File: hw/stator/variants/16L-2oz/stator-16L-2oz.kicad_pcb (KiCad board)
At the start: 16 copper layers, 175 x 175 mm, 1 part

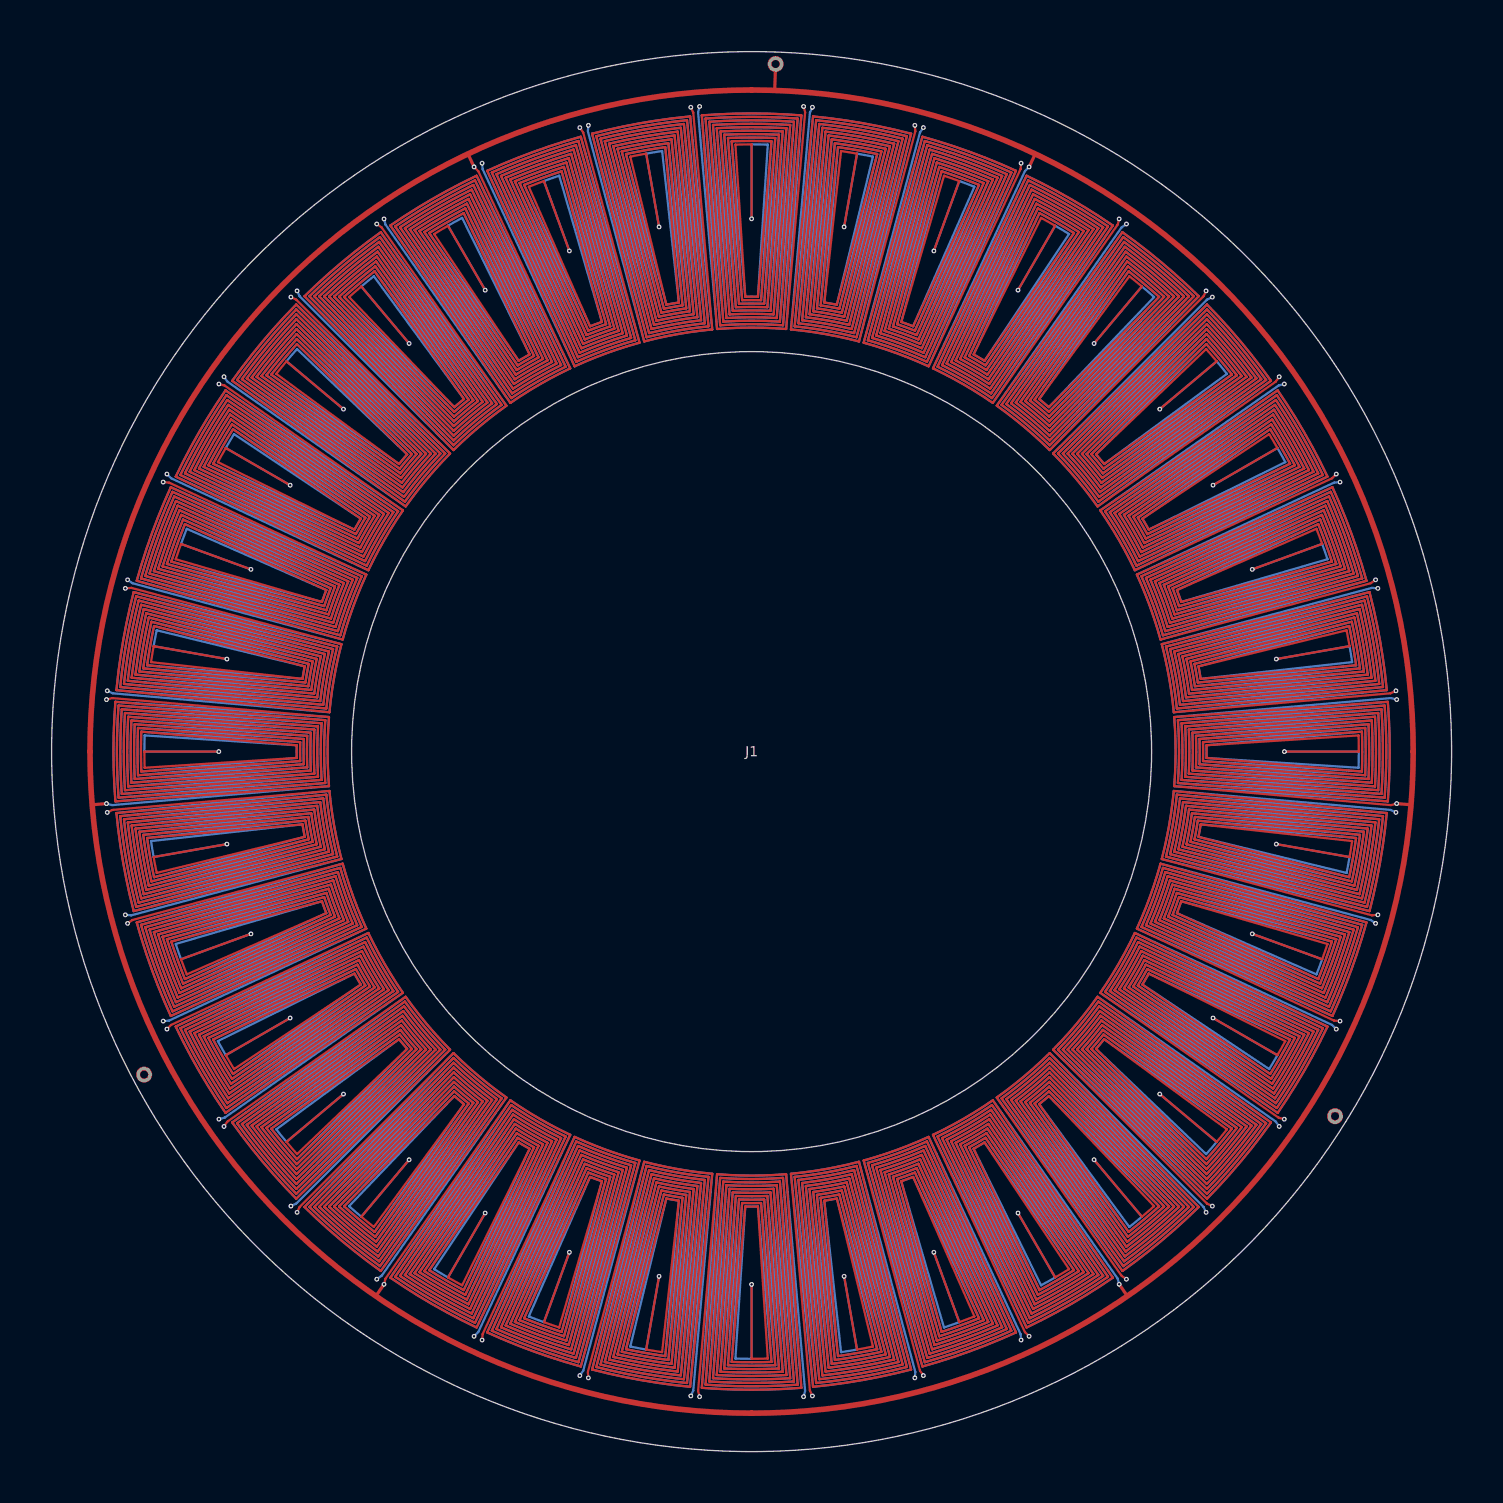
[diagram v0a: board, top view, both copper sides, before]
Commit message: Round 9 in progress: stator layout v2 (coils to r 84.6, +14 % torque), N-S rotor comparison, base as cheap parts, BOM at 20 and 100 units
Co-Authored-By: Claude Fable 5.1 <noreply@anthropic.com>
Claude-Session: https://claude.ai/code/session_01RhbB1sts16H7Chkqp6ycKd
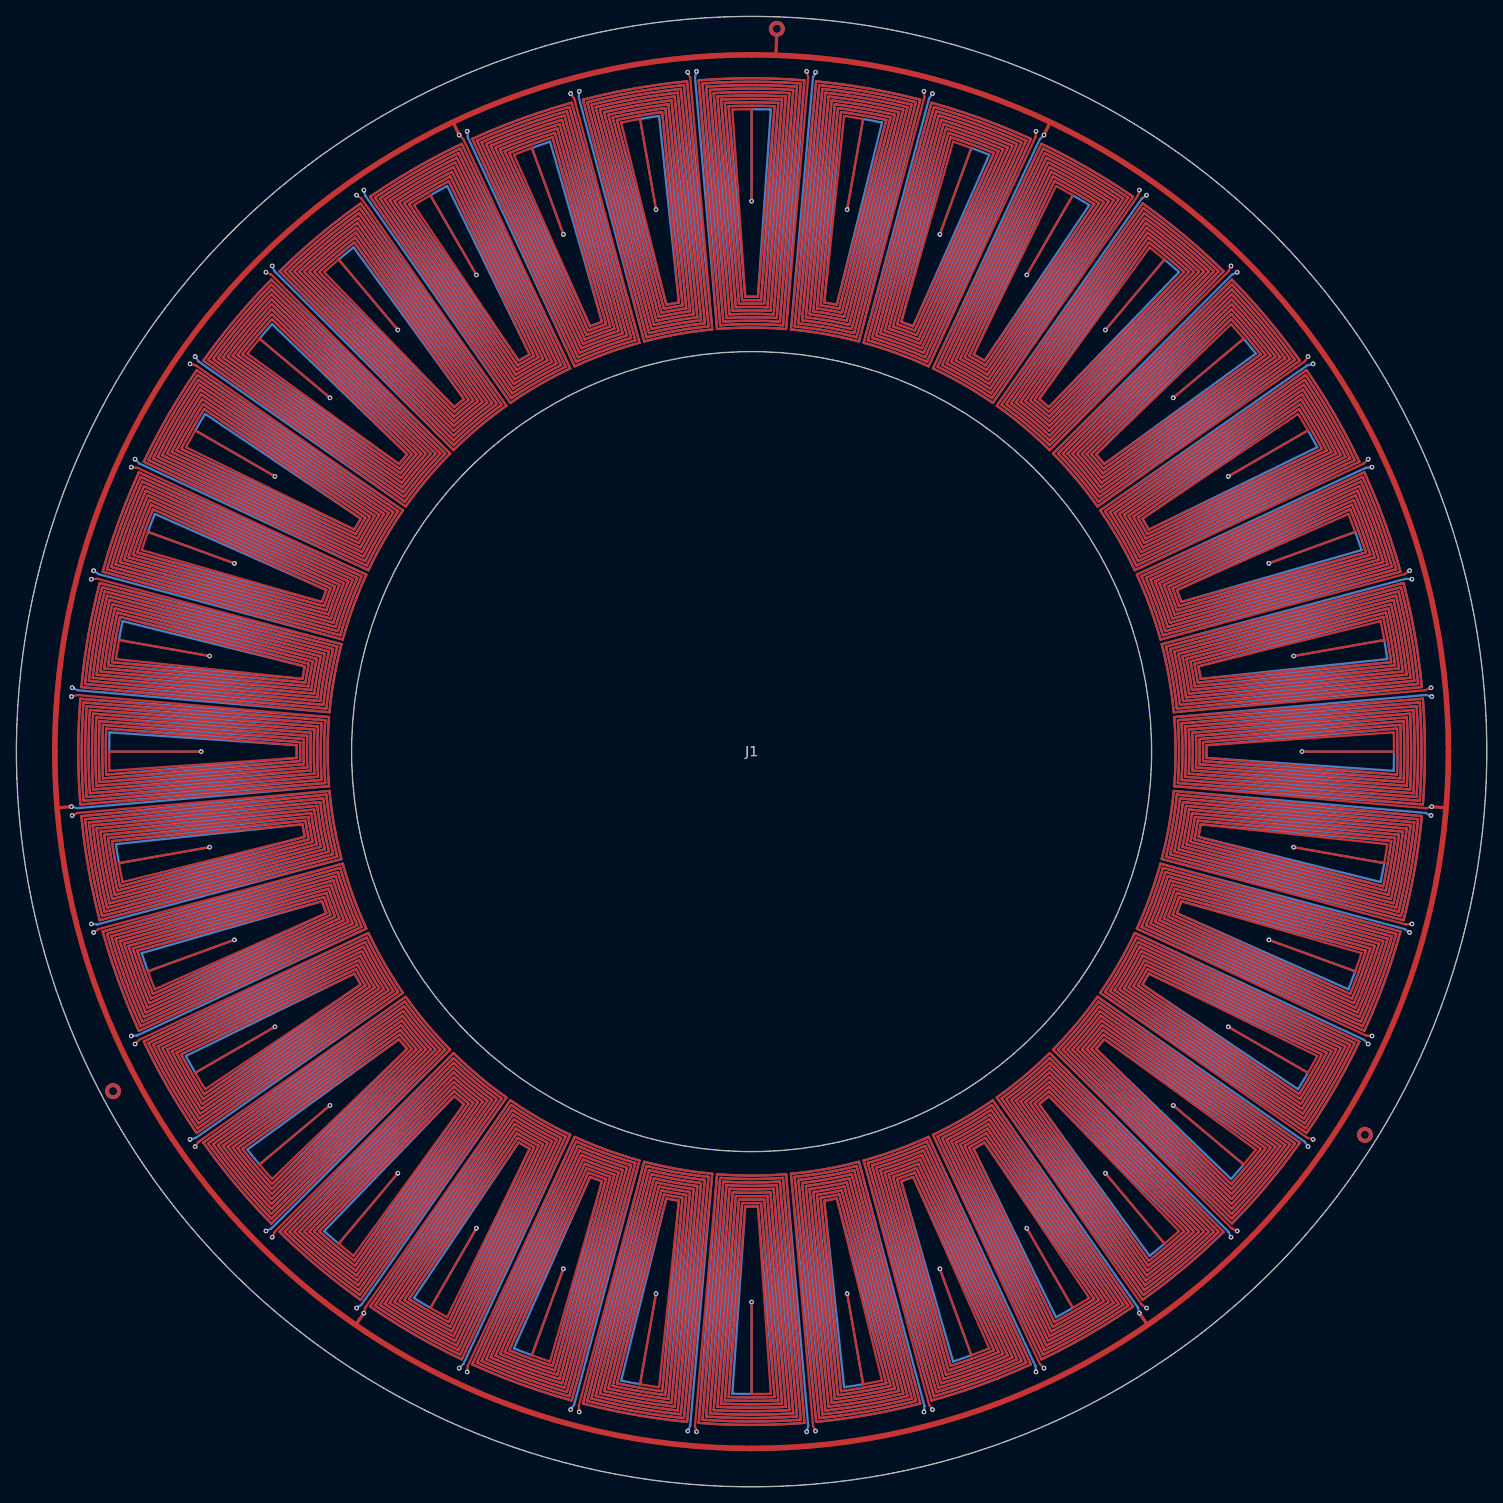
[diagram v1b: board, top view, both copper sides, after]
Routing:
- net (no net): track 356283.9 -> 412992.6 mm
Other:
- board size 175 x 175 mm -> 183.8 x 183.8 mm
